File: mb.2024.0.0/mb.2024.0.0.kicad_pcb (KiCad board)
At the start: 2 copper layers, 247.8 x 124 mm, 96 parts, among them J1 DSP_out_12v_GND, J10 DSP+, J11 Screw_Terminal_VMN, J12 Conn_01x08_Female, J13 Connector_I2C_for_mux, J14 Conn_01x02_Female, J15 Conn_01x08_Female, J16 RX_bat, J17 DSP GND, J18 ELEC_M, J19 ELEC_N, J2 DPS5005_input_0_to_50V, J20 shunt +, J21 shunt -, J3 Screw_Terminal_AB, J4 Conn_01x08_Female, J5 Conn_01x04_Female, J6 Conn_01x08_Female, J7 Raspberry_Pi_2_3, J8 Connector_I2C_for_MCP23008, J9 TX_bat, K1 G5LE-1, K2 G5LE-1, K3 G5LE-1, K4 G5LE-1, K5 G5LE-1, K6 G5LE-1, Q1 ZVN4206ASTZ, Q2 ZVN4206ASTZ, Q3 ZVN4206ASTZ, Q4 ZVN4206ASTZ, Q5 ZVN4206ASTZ, Q6 ZVN4206ASTZ, U1 MCP23008-xP, U2 OP07, U3 24LC02, U4 1115-Adress=0X49, U5 1115-Adress=0X48, U6 OP07, U7 OP07

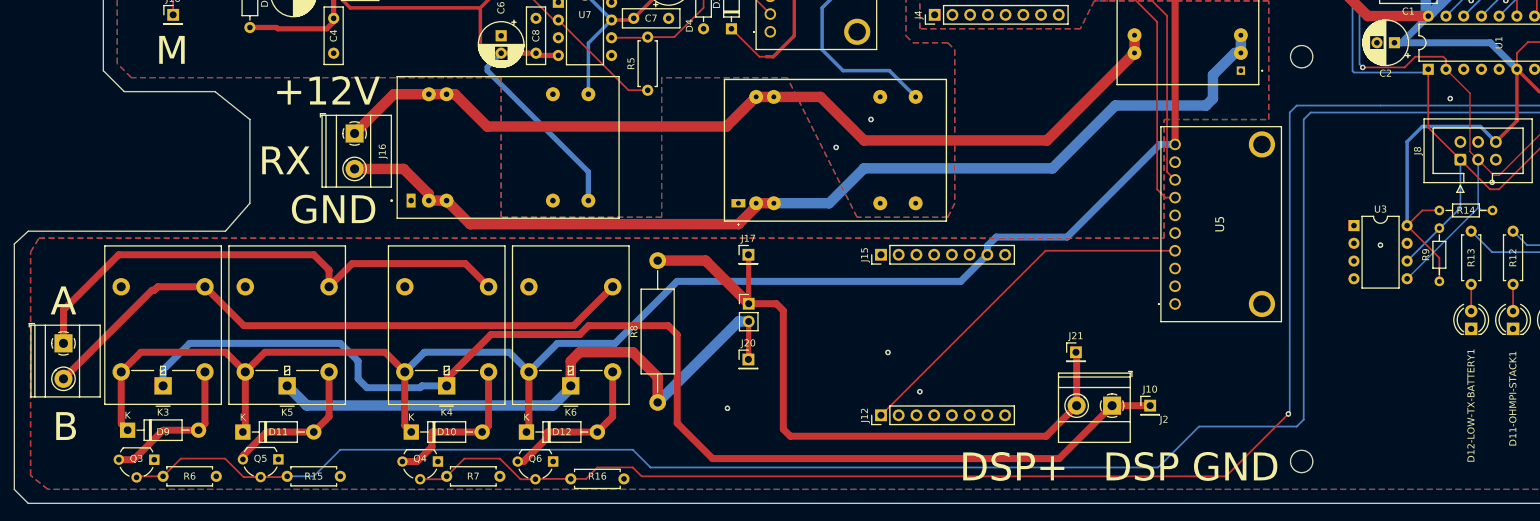
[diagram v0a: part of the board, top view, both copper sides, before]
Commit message: update measurement board schematics and circuit
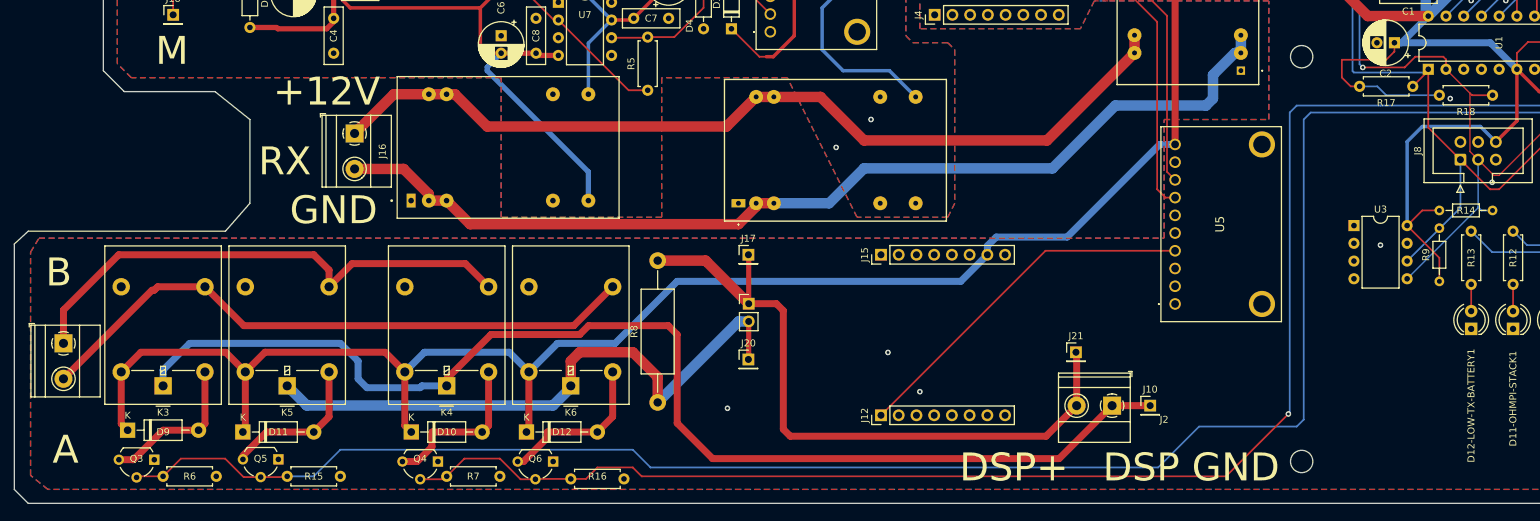
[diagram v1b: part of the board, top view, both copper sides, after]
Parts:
- added R17: 4.7K, Resistor_THT:R_Axial_DIN0207_L6.3mm_D2.5mm_P7.62mm_Horizontal, F.Cu at (214.6, 95.2)
- added R18: 4.7K, Resistor_THT:R_Axial_DIN0207_L6.3mm_D2.5mm_P7.62mm_Horizontal, F.Cu at (226.1, 96.5)
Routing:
- net 5VD: track 504.3 -> 531.1 mm
- net SCL1: track 181.2 -> 184.6 mm
- net SDA1: track 205.3 -> 208.7 mm

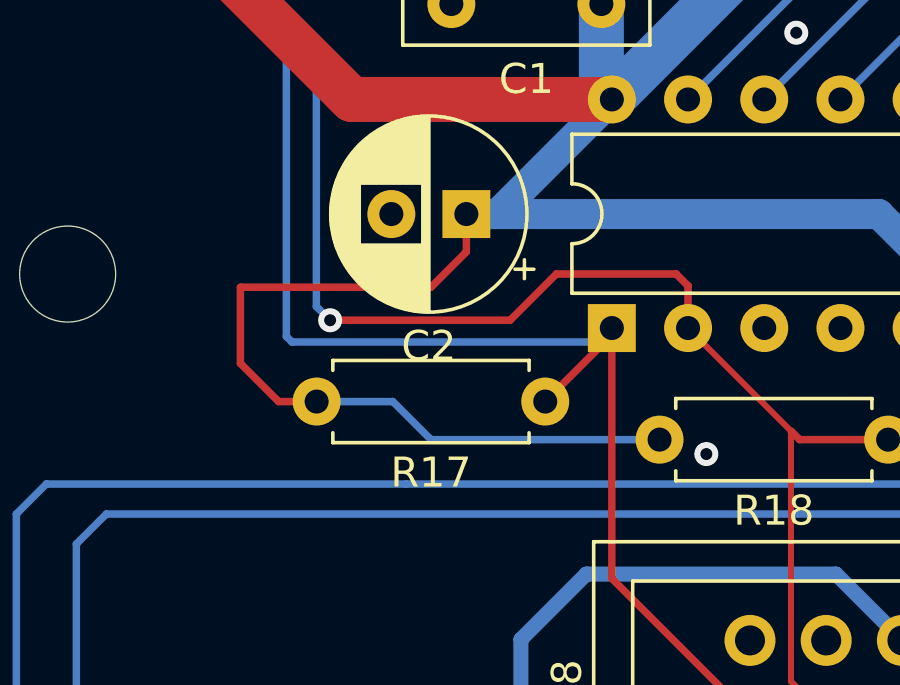
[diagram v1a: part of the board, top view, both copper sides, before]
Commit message: update measurement board schematics and circuit
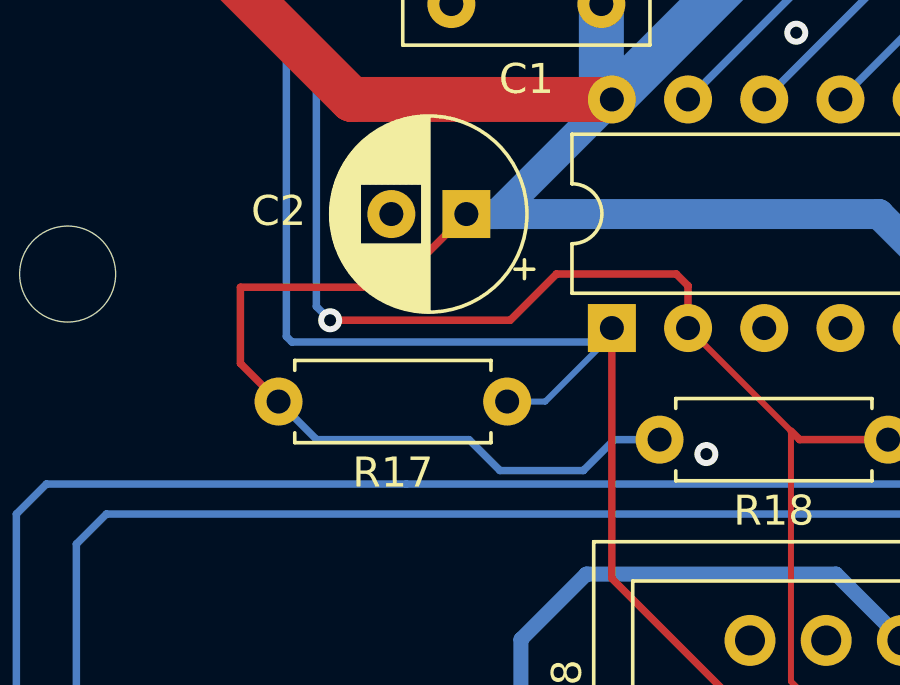
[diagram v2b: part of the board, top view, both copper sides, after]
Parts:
- moved R17 1.27 mm to (213.4, 95.2)
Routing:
- net SCL1: track 184.6 -> 185.2 mm
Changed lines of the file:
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@@
     (property "Sheetname" "")
     (attr through_hole)
-    (fp_text reference "C2" (at 1.25 -4.4) (layer "F.SilkS")
+    (fp_text reference "C2" (at 6.26 0.1) (layer "F.SilkS")
       (effects (font (size 1 1) (thickness 0.15)))
     )
@@
   )
   (footprint "Resistor_THT:R_Axial_DIN0207_L6.3mm_D2.5mm_P7.62mm_Horizontal" (layer "F.Cu")
-    (at 214.63 95.25 180)
+    (at 213.36 95.25 180)
     (descr "Resistor, Axial_DIN0207 series, Axial, Horizontal, pin pitch=7.62mm, 0.25W = 1/4W, length*diameter=6.3*2.5mm^2, http://cdn-reichelt.de/documents/datenblatt/B400/1_4W%23YAG.pdf")
     (tags "Resistor Axial_DIN0207 series Axial Horizontal pin pitch 7.62mm 0.25W = 1/4W length 6.3mm diameter 2.5mm")
@@
   (segment (start 47.34 136.1675) (end 47.34 144.43) (width 1) (layer "F.Cu") (net 1))
   (segment (start 47.34 136.1675) (end 50.1575 133.35) (width 1) (layer "F.Cu") (net 1))
-  (segment (start 207.01 95.25) (end 205.74 95.25) (width 0.25) (layer "F.Cu") (net 1))
+  (segment (start 204.47 93.98) (end 205.74 95.25) (width 0.25) (layer "F.Cu") (net 1))
   (segment (start 197.92 54.08) (end 197.92 61) (width 1) (layer "F.Cu") (net 1))
   (segment (start 67.3825 133.35) (end 70.2 136.1675) (width 1) (layer "F.Cu") (net 1))
@@
   (segment (start 174.76 67.6) (end 166.965 67.6) (width 0.5) (layer "F.Cu") (net 1))
   (segment (start 229.55 90.49) (end 229.55 92.8) (width 0.25) (layer "F.Cu") (net 1))
-  (segment (start 204.47 93.98) (end 204.47 91.44) (width 0.25) (layer "F.Cu") (net 1))
   (segment (start 87.98 136.1675) (end 87.98 144.43) (width 1) (layer "F.Cu") (net 1))
   (segment (start 248.4025 76.205) (end 246.385 76.205) (width 0.25) (layer "F.Cu") (net 1))
   (segment (start 181.36 61) (end 174.76 67.6) (width 1.5) (layer "F.Cu") (net 1))
   (segment (start 70.2 143.86) (end 71.12 144.78) (width 1) (layer "F.Cu") (net 1))
+  (segment (start 209.56 91.44) (end 204.47 91.44) (width 0.25) (layer "F.Cu") (net 1))
   (segment (start 44.5225 133.35) (end 47.34 136.1675) (width 1) (layer "F.Cu") (net 1))
   (segment (start 29.56 143.5975) (end 30.48 144.5175) (width 1) (layer "F.Cu") (net 1))
-  (segment (start 210.82 91.44) (end 212 90.26) (width 0.25) (layer "F.Cu") (net 1))
   (segment (start 180.571 72.771) (end 175.4 67.6) (width 1) (layer "F.Cu") (net 1))
   (segment (start 218.44 113.03) (end 215.99 113.03) (width 0.25) (layer "F.Cu") (net 1))
   (segment (start 222 59.92) (end 220.92 61) (width 1) (layer "F.Cu") (net 1))
-  (segment (start 212 90.26) (end 212 89) (width 0.25) (layer "F.Cu") (net 1))
   (segment (start 87.98 144.43) (end 87.63 144.78) (width 1) (layer "F.Cu") (net 1))
   (segment (start 246.38 76.2) (end 242.57 80.01) (width 0.25) (layer "F.Cu") (net 1))
   (segment (start 197.92 61) (end 181.36 61) (width 1.5) (layer "F.Cu") (net 1))
   (segment (start 213.82 115.2) (end 218.44 119.82) (width 0.25) (layer "F.Cu") (net 1))
+  (segment (start 212 89) (end 209.56 91.44) (width 0.25) (layer "F.Cu") (net 1))
   (segment (start 166.965 67.6) (end 161.365 62) (width 0.5) (layer "F.Cu") (net 1))
-  (segment (start 205.74 95.25) (end 204.47 93.98) (width 0.25) (layer "F.Cu") (net 1))
   (segment (start 180.571 103.57) (end 180.571 72.771) (width 1) (layer "F.Cu") (net 1))
   (segment (start 249.04 94.697919) (end 249.04 95.9) (width 0.5) (layer "F.Cu") (net 1))
   (segment (start 50.1575 133.35) (end 67.3825 133.35) (width 1) (layer "F.Cu") (net 1))
   (segment (start 70.2 136.1675) (end 70.2 143.86) (width 1) (layer "F.Cu") (net 1))
+  (segment (start 204.47 91.44) (end 204.47 93.98) (width 0.25) (layer "F.Cu") (net 1))
   (segment (start 216.85 85.18) (end 208.18 85.18) (width 1.5) (layer "F.Cu") (net 1))
   (segment (start 197.92 74.92) (end 197.92 61) (width 1.5) (layer "F.Cu") (net 1))
@@
   (segment (start 229.55 100.1975) (end 226.535 103.2125) (width 0.5) (layer "F.Cu") (net 1))
   (segment (start 47.34 144.43) (end 46.99 144.78) (width 1) (layer "F.Cu") (net 1))
-  (segment (start 204.47 91.44) (end 210.82 91.44) (width 0.25) (layer "F.Cu") (net 1))
   (segment (start 215.99 113.03) (end 213.82 115.2) (width 0.25) (layer "F.Cu") (net 1))
   (segment (start 231.14 88.9) (end 229.55 90.49) (width 0.25) (layer "F.Cu") (net 1))
@@
   (segment (start 216.5 82) (end 216.5 84.83) (width 1.5) (layer "B.Cu") (net 1))
   (segment (start 213.82 115.2) (end 213.82 103.18) (width 0.5) (layer "B.Cu") (net 1))
+  (segment (start 207.01 96.52) (end 212.09 96.52) (width 0.25) (layer "B.Cu") (net 1))
+  (segment (start 205.74 95.25) (end 207.01 96.52) (width 0.25) (layer "B.Cu") (net 1))
+  (segment (start 215.9 97.55) (end 216.93 96.52) (width 0.25) (layer "B.Cu") (net 1))
   (segment (start 224.3225 101) (end 226.535 103.2125) (width 0.5) (layer "B.Cu") (net 1))
   (segment (start 153.67 118.11) (end 154.94 116.84) (width 1) (layer "B.Cu") (net 1))
-  (segment (start 209.55 95.25) (end 210.82 96.52) (width 0.25) (layer "B.Cu") (net 1))
   (segment (start 100.33 132.08) (end 92.0675 132.08) (width 1) (layer "B.Cu") (net 1))
-  (segment (start 210.82 96.52) (end 218.44 96.52) (width 0.25) (layer "B.Cu") (net 1))
   (segment (start 216 101) (end 224.3225 101) (width 0.5) (layer "B.Cu") (net 1))
   (segment (start 212 89) (end 225.75 89) (width 1) (layer "B.Cu") (net 1))
   (segment (start 85.1625 133.35) (end 87.98 136.1675) (width 1) (layer "B.Cu") (net 1))
+  (segment (start 213.12 97.55) (end 215.9 97.55) (width 0.25) (layer "B.Cu") (net 1))
+  (segment (start 216.93 96.52) (end 218.44 96.52) (width 0.25) (layer "B.Cu") (net 1))
   (segment (start 213.03 89) (end 216.85 85.18) (width 1) (layer "B.Cu") (net 1))
   (segment (start 178.37 103.57) (end 165.1 116.84) (width 1) (layer "B.Cu") (net 1))
   (segment (start 154.94 116.84) (end 165.1 116.84) (width 1) (layer "B.Cu") (net 1))
-  (segment (start 207.01 95.25) (end 209.55 95.25) (width 0.25) (layer "B.Cu") (net 1))
   (segment (start 153.67 119.38) (end 149.86 123.19) (width 1) (layer "B.Cu") (net 1))
   (segment (start 149.86 123.19) (end 109.22 123.19) (width 1) (layer "B.Cu") (net 1))
@@
   (segment (start 216.5 84.83) (end 216.85 85.18) (width 1.5) (layer "B.Cu") (net 1))
   (segment (start 212 89) (end 213.03 89) (width 1) (layer "B.Cu") (net 1))
+  (segment (start 212.09 96.52) (end 213.12 97.55) (width 0.25) (layer "B.Cu") (net 1))
   (segment (start 73.0175 133.35) (end 85.1625 133.35) (width 1) (layer "B.Cu") (net 1))
   (segment (start 153.67 119.38) (end 153.67 118.11) (width 1) (layer "B.Cu") (net 1))
@@
   (segment (start 179.413989 107.492989) (end 179.413989 85.128989) (width 0.25) (layer "F.Cu") (net 8))
   (segment (start 225.7025 110) (end 221.455 105.7525) (width 0.25) (layer "F.Cu") (net 8))
-  (segment (start 216.85 92.8) (end 216.85 93.03) (width 0.25) (layer "F.Cu") (net 8))
   (segment (start 227 110) (end 225.7025 110) (width 0.25) (layer "F.Cu") (net 8))
   (segment (start 236.02 100.98) (end 227 110) (width 0.25) (layer "F.Cu") (net 8))
   (segment (start 216.85 92.8) (end 216.85 101.1475) (width 0.25) (layer "F.Cu") (net 8))
-  (segment (start 216.85 93.03) (end 214.63 95.25) (width 0.25) (layer "F.Cu") (net 8))
   (segment (start 180.571 108.65) (end 179.413989 107.492989) (width 0.25) (layer "F.Cu") (net 8))
   (segment (start 216.85 101.1475) (end 221.455 105.7525) (width 0.25) (layer "F.Cu") (net 8))
@@
   (segment (start 206.184511 93.264511) (end 216.385489 93.264511) (width 0.25) (layer "B.Cu") (net 8))
   (segment (start 221.455 112.645) (end 221.455 105.7525) (width 0.25) (layer "B.Cu") (net 8))
+  (segment (start 214.63 95.25) (end 216.85 93.03) (width 0.2) (layer "B.Cu") (net 8))
   (segment (start 156.285 62) (end 169.1425 74.8575) (width 0.25) (layer "B.Cu") (net 8))
   (segment (start 213.82 120.28) (end 221.455 112.645) (width 0.25) (layer "B.Cu") (net 8))
   (segment (start 169.1425 74.8575) (end 172.285 78) (width 0.25) (layer "B.Cu") (net 8))
   (segment (start 201 78) (end 206 83) (width 0.25) (layer "B.Cu") (net 8))
+  (segment (start 216.85 93.03) (end 216.85 92.8) (width 0.2) (layer "B.Cu") (net 8))
+  (segment (start 213.36 95.25) (end 214.63 95.25) (width 0.2) (layer "B.Cu") (net 8))
   (segment (start 206 93.08) (end 206.184511 93.264511) (width 0.25) (layer "B.Cu") (net 8))
   (segment (start 172.285 78) (end 201 78) (width 0.25) (layer "B.Cu") (net 8))
   (segment (start 206 83) (end 206 93.08) (width 0.25) (layer "B.Cu") (net 8))
-  (segment (start 216.385489 93.264511) (end 216.85 92.8) (width 0.25) (layer "B.Cu") (net 8))
   (segment (start 92.2 85.74) (end 102.27 95.81) (width 0.25) (layer "F.Cu") (net 10))
   (segment (start 86.81 81) (end 91.55 85.74) (width 0.25) (layer "F.Cu") (net 10))
